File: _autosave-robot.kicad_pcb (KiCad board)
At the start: 4 copper layers, 132 x 60.2 mm, 170 parts, among them J1 USB_C_Receptacle_USB2.0_16P, J10 5V, J2 Batt-Cell Connector, J3 Batt Connector, J4 DVR FOUT, J5 3.3V, J6 DRV BOUT, J7 UART, J8 I2C, J9 5way Tracing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

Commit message: Update gerber file
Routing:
- net /STDBY: track 18.1 -> 19.2 mm
- net /ESP32-C6-mini/D+: track 128.1 -> 129.2 mm
- net /ESP32-C6-mini/B_BIN1: track 114.1 -> 113.5 mm

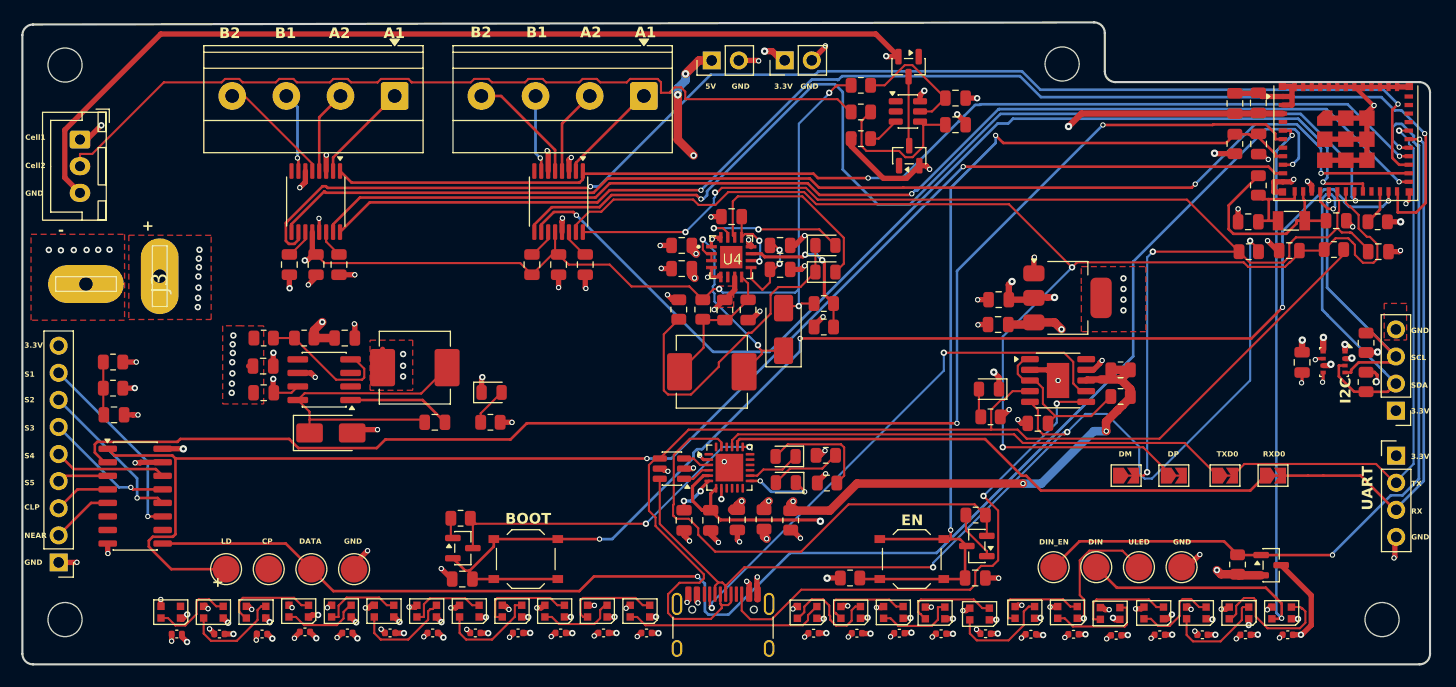
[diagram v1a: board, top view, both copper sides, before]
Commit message: Refine PCB layout: shift status LED for better visibility
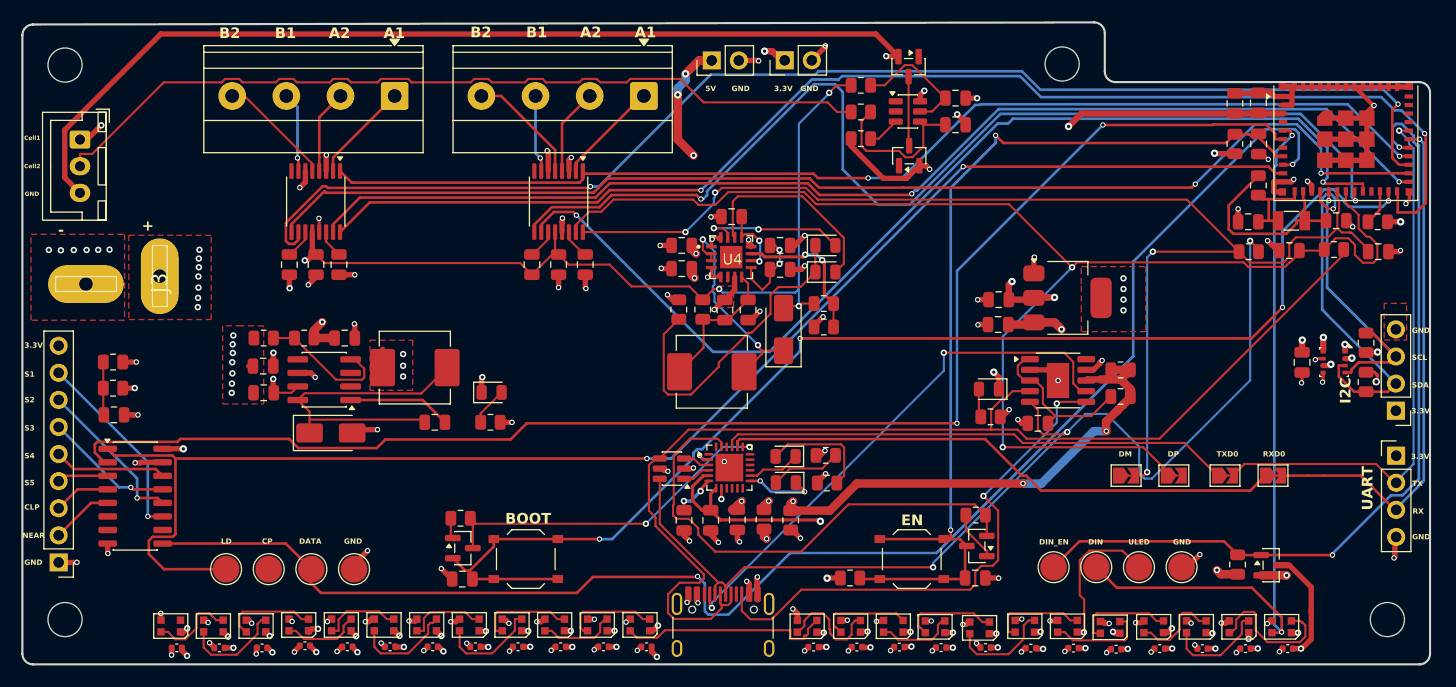
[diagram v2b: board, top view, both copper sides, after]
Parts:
- moved C49 1.30 mm to (204.7, 113.6)
- moved C50 1.30 mm to (200.8, 113.6)
- moved C51 1.30 mm to (196.7, 113.6)
- moved C61 1.30 mm to (149.0, 113.5)
- moved C40 1.30 mm to (241.2, 113.7)
- moved C41 1.30 mm to (237.2, 113.7)
- moved C42 1.30 mm to (233.2, 113.7)
- moved C43 1.30 mm to (229.2, 113.7)
- moved C44 1.30 mm to (225.1, 113.8)
- moved C45 1.30 mm to (221.1, 113.7)
- moved C46 1.30 mm to (217.1, 113.7)
- moved C47 1.30 mm to (212.8, 113.6)
- moved C48 1.30 mm to (208.7, 113.6)
- moved C52 1.30 mm to (181.0, 113.6)
- moved C53 1.30 mm to (177.0, 113.6)
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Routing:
- net /ESP32-C6-mini/user_interface/ULED: track 53.3 -> 57.5 mm
- net /ESP32-C6-mini/DIN: track 68.4 -> 70.4 mm
- net /Cell2: track 81.0 -> 79.6 mm
- net Net-(D21-DOUT): track 18.8 -> 20.1 mm
- net /ESP32-C6-mini/DATA: track 140.2 -> 141.2 mm
- net +5V: track 28.2 -> 28.5 mm, vias 10 -> 11
